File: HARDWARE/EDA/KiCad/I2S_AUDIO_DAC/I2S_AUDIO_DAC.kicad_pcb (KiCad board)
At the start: 2 copper layers, 28 parts, among them J1 Conn_01x07_Male, J2 Conn_01x010_Male, U1 L78L33_TO92, U2 UDA1334ATS

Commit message: add led to schematic and adjust pcb
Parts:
- added D1: PW, LED_THT:LED_D5.0mm, F.Cu at (178.8, 84.0)
- added D2: VDD, LED_THT:LED_D5.0mm, F.Cu at (178.8, 76.5)
- added R13: 100R, Resistor_THT:R_Axial_DIN0207_L6.3mm_D2.5mm_P7.62mm_Horizontal, F.Cu at (189.4, 84.0)
- added R14: 15R, Resistor_THT:R_Axial_DIN0207_L6.3mm_D2.5mm_P7.62mm_Horizontal, F.Cu at (189.4, 76.5)
- moved C2 18.2 mm to (191.5, 106.8), turned to 270 degrees
- moved C5 16.2 mm to (186.3, 112.9), turned to 270 degrees
- moved C1 15.9 mm to (190.1, 103.0), turned to 0 degrees
- moved R3 14.2 mm to (189.0, 105.0), turned to 270 degrees
- moved C9 13.0 mm to (182.2, 112.9), turned to 270 degrees
- moved U2 12.3 mm to (185.8, 99.5), turned to 270 degrees
- moved C6 9.64 mm to (185.5, 105.3), turned to 270 degrees
- moved R9 8.38 mm to (196.7, 74.0)
- moved C10 6.17 mm to (183.0, 105.3), turned to 270 degrees
- moved R7 5.83 mm to (199.2, 74.0)
- moved R8 4.44 mm to (209.2, 74.0)
- moved R11 3.28 mm to (201.7, 74.0)
- moved R6 2.04 mm to (180.0, 105.0), turned to 270 degrees
- moved C7 1.90 mm to (204.0, 107.1), turned to 180 degrees
- moved R12 1.78 mm to (206.7, 74.0)
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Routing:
- net 0: track 52.9 -> 139.8 mm
- net analog_supply_voltage: track 32.2 -> 75.6 mm
- net /BITCLK_IN: track 0.00 -> 39.0 mm
- net /WORDSEL_IN: track 0.00 -> 34.7 mm, vias 0 -> 2
- net /DATA_IN: track 0.00 -> 34.4 mm, vias 0 -> 2
- net VOUTL: track 0.00 -> 29.1 mm
- net VOUTR: track 0.00 -> 26.5 mm
- net /DEEM-CLKOUT: track 0.00 -> 20.8 mm
- net /PLL_IN: track 0.00 -> 17.2 mm
- net /SFOR0: track 0.00 -> 14.2 mm
- net VDDD: track 11.7 -> 23.9 mm
- net /MUTE: track 0.00 -> 11.8 mm
- net /SFOR1: track 0.00 -> 9.33 mm
- net /SYSCLK_IN: track 0.00 -> 6.64 mm
- net VREF_DAC: track 4.17 -> 9.60 mm
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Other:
- net class Default: clearance 0.25 -> 0.5
- rule trace_clearance: 0.25 -> 0.5

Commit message: pcb finished
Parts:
- moved R14 14.8 mm to (179.1, 87.1), turned to 270 degrees
- moved D1 7.90 mm to (177.8, 76.2), turned to 0 degrees
- moved R13 6.74 mm to (184.1, 79.8), turned to 270 degrees
- moved D2 5.06 mm to (179.1, 81.5), turned to 270 degrees
- moved C1 1.75 mm to (190.1, 101.2)
- moved C10 1.75 mm to (183.0, 103.5)
- moved C2 1.75 mm to (191.5, 105.0)
- moved C5 1.75 mm to (186.3, 111.2)
- moved C6 1.75 mm to (185.5, 103.6)
- moved C9 1.75 mm to (182.2, 111.2)
- moved R3 1.75 mm to (189.0, 103.2)
- moved R6 1.75 mm to (180.0, 103.3)
- moved U2 1.75 mm to (185.8, 97.8)
- moved C12 0.73 mm to (199.4, 98.0)
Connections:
- D1 pad 1: Net-(D1-Pad1) -> 0
- D1 pad 2: VDC -> Net-(D1-Pad2)
- D2 pad 1: Net-(D2-Pad1) -> 0
- D2 pad 2: analog_supply_voltage -> Net-(D2-Pad2)
- R13 pad 1: 0 -> Net-(D1-Pad2)
- R13 pad 2: Net-(D1-Pad1) -> VDC
- R14 pad 1: 0 -> Net-(D2-Pad2)
- R14 pad 2: Net-(D2-Pad1) -> analog_supply_voltage
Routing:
- net 0: track 139.8 -> 196.7 mm
- net /SYSCLK_IN: track 6.64 -> 50.7 mm, vias 0 -> 2
- net /SFOR1: track 9.33 -> 47.8 mm, vias 0 -> 2
- net /MUTE: track 11.8 -> 45.2 mm, vias 0 -> 2
- net VDC: track 5.67 -> 36.8 mm
- net /SFOR0: track 14.2 -> 39.6 mm, vias 0 -> 2
- net /PLL_IN: track 17.2 -> 40.5 mm, vias 0 -> 2
- net /DEEM-CLKOUT: track 20.8 -> 40.9 mm, vias 0 -> 2
- net VOUTR: track 26.5 -> 34.7 mm
- net /BITCLK_IN: track 39.0 -> 46.1 mm, vias 0 -> 2
- net Net-(D1-Pad2): track 0.00 -> 5.22 mm
- net /DATA_IN: track 34.4 -> 38.4 mm, vias 2 -> 1
- net /WORDSEL_IN: track 34.7 -> 38.5 mm, vias 2 -> 1
- net analog_supply_voltage: track 75.6 -> 79.1 mm
- net Net-(D2-Pad2): track 0.00 -> 2.98 mm
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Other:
- board outline added: 42 x 49.5 mm
- net class Default: clearance 0.5 -> 0.25
- rule trace_clearance: 0.5 -> 0.25

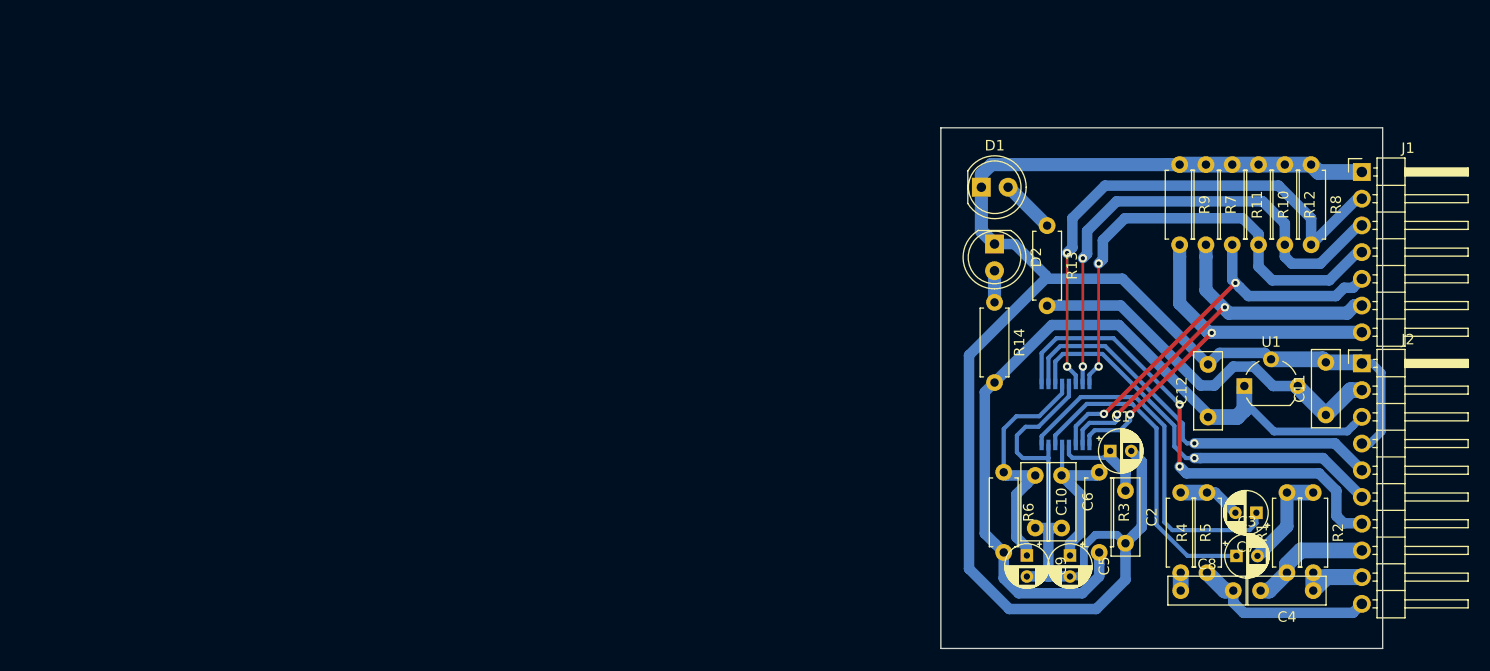
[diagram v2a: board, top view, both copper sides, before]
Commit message: psb page sheet configured
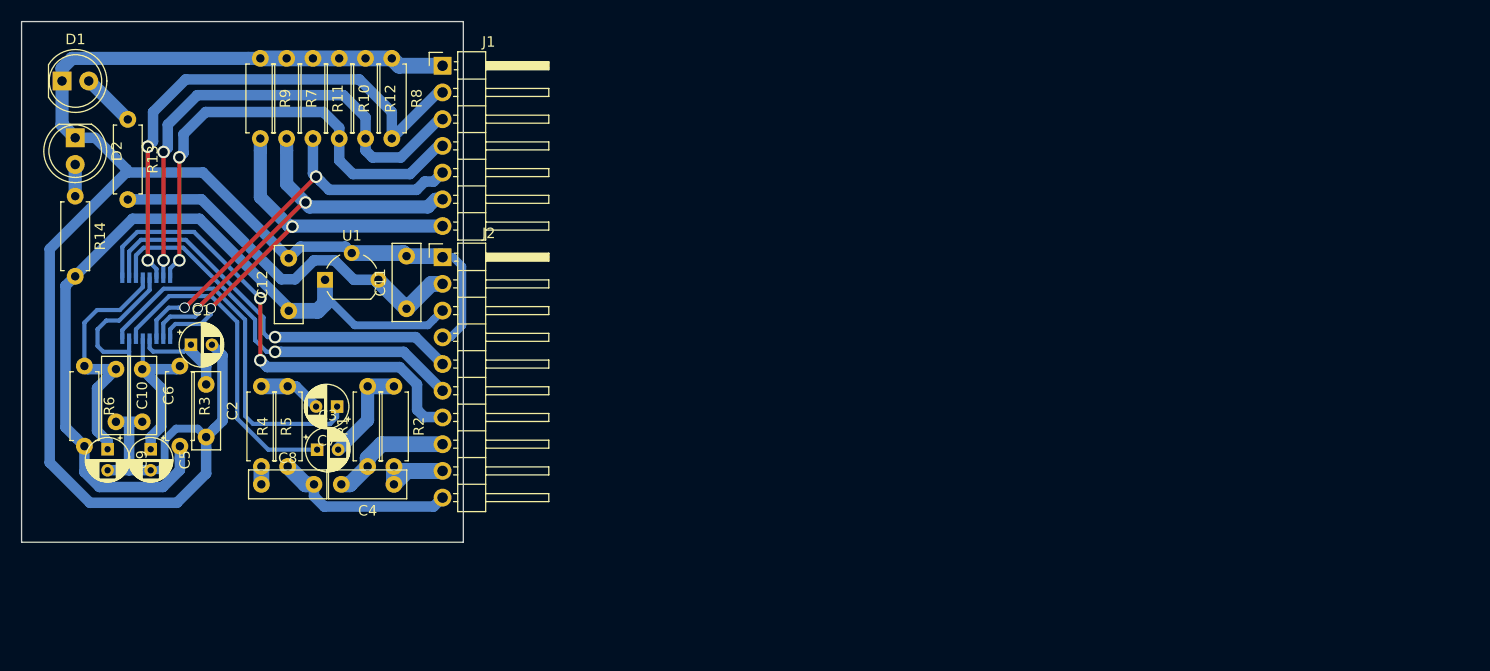
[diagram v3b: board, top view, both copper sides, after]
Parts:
- moved C2 88.0 mm to (104.1, 94.9)
- moved R3 88.0 mm to (101.6, 93.2)
- moved C12 88.0 mm to (112.0, 87.9)
- moved C4 88.0 mm to (122.0, 104.4)
- moved C5 88.0 mm to (98.9, 101.1)
- moved C7 88.0 mm to (116.6, 97.0)
- moved C8 88.0 mm to (109.4, 104.4)
- moved C9 88.0 mm to (94.8, 101.1)
- moved J1 88.0 mm to (126.6, 64.6)
- moved J2 88.0 mm to (126.6, 82.8)
- moved R1 88.0 mm to (119.5, 102.7)
- moved R2 88.0 mm to (122.0, 95.1)
- moved R4 88.0 mm to (111.9, 102.7)
- moved R5 88.0 mm to (109.4, 95.1)
- moved C1 88.0 mm to (102.7, 91.1)
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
